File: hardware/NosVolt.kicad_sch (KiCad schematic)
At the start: 10 parts, among them J101 INPUTS, J102 OUTPUTS, SW101 SW_Reset, SW102 SSSS811101, U101 ESP32-S3-WROOM-1

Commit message: Fixes
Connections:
- no-connect marks 0 -> 6
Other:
- sheet USB_LDO ports: added 5V; removed none
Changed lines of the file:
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@@
 		(color 0 0 0 0)
 	)
+	(no_connect
+		(at 137.16 147.32)
+	)
+	(no_connect
+		(at 62.23 74.93)
+	)
+	(no_connect
+		(at 68.58 118.11)
+	)
+	(no_connect
+		(at 68.58 143.51)
+	)
+	(no_connect
+		(at 137.16 173.99)
+	)
+	(no_connect
+		(at 137.16 121.92)
+	)
 	(wire
 		(pts
@@
 	(wire
 		(pts
+			(xy 130.81 173.99) (xy 137.16 173.99)
+		)
+		(stroke
+			(width 0)
+			(type default)
+		)
+	)
+	(wire
+		(pts
 			(xy 67.31 147.32) (xy 82.55 147.32)
 		)
@@
 	(wire
 		(pts
+			(xy 130.81 147.32) (xy 137.16 147.32)
+		)
+		(stroke
+			(width 0)
+			(type default)
+		)
+	)
+	(wire
+		(pts
 			(xy 69.85 163.83) (xy 69.85 149.86)
 		)
@@
 	(wire
 		(pts
+			(xy 62.23 118.11) (xy 68.58 118.11)
+		)
+		(stroke
+			(width 0)
+			(type default)
+		)
+	)
+	(wire
+		(pts
 			(xy 77.47 85.09) (xy 82.55 85.09)
 		)
@@
 	(wire
 		(pts
+			(xy 62.23 143.51) (xy 68.58 143.51)
+		)
+		(stroke
+			(width 0)
+			(type default)
+		)
+	)
+	(wire
+		(pts
 			(xy 260.35 52.07) (xy 270.51 52.07)
 		)
@@
 	(wire
 		(pts
+			(xy 55.88 74.93) (xy 62.23 74.93)
+		)
+		(stroke
+			(width 0)
+			(type default)
+		)
+	)
+	(wire
+		(pts
 			(xy 88.9 121.92) (xy 88.9 147.32)
 		)
@@
 	(wire
 		(pts
+			(xy 130.81 121.92) (xy 137.16 121.92)
+		)
+		(stroke
+			(width 0)
+			(type default)
+		)
+	)
+	(wire
+		(pts
 			(xy 57.15 36.83) (xy 57.15 35.56)
 		)
@@
 	)
 	(sheet
-		(at 43.18 74.93)
-		(size 12.7 10.16)
+		(at 43.18 72.39)
+		(size 12.7 12.7)
 		(exclude_from_sim no)
 		(in_bom yes)
@@
 		)
 		(property "Sheetname" "USB_LDO"
-			(at 43.18 70.866 0)
+			(at 43.18 68.326 0)
 			(effects
 				(font
@@
 		)
 		(property "Sheetfile" "USB_LDO.kicad_sch"
-			(at 42.672 72.39 0)
+			(at 42.672 69.85 0)
 			(effects
 				(font
@@
 			(effects
 				(font
+					(size 1.27 1.27)
+				)
+				(justify right)
+			)
+		)
+		(pin "5V" output
+			(at 55.88 74.93 0)
+			(effects
+				(font

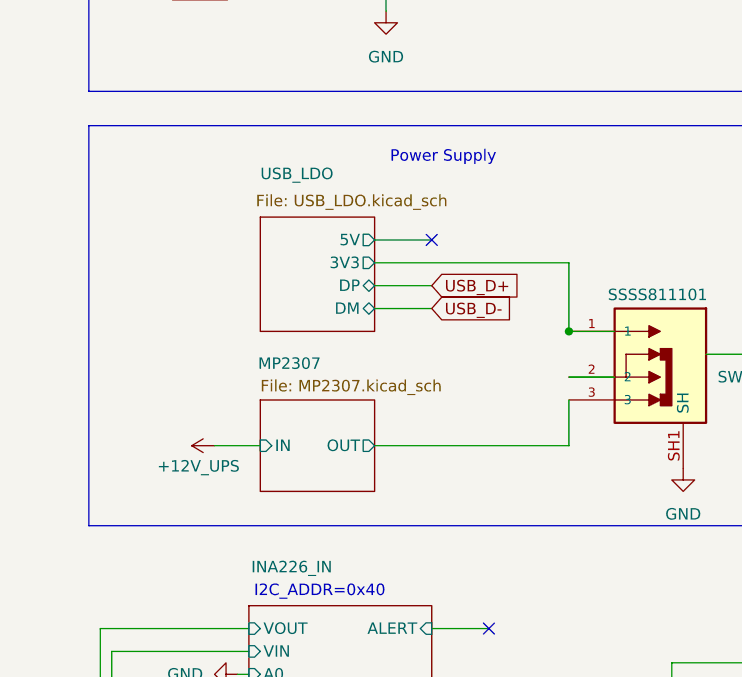
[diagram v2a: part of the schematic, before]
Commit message: ldo optimization
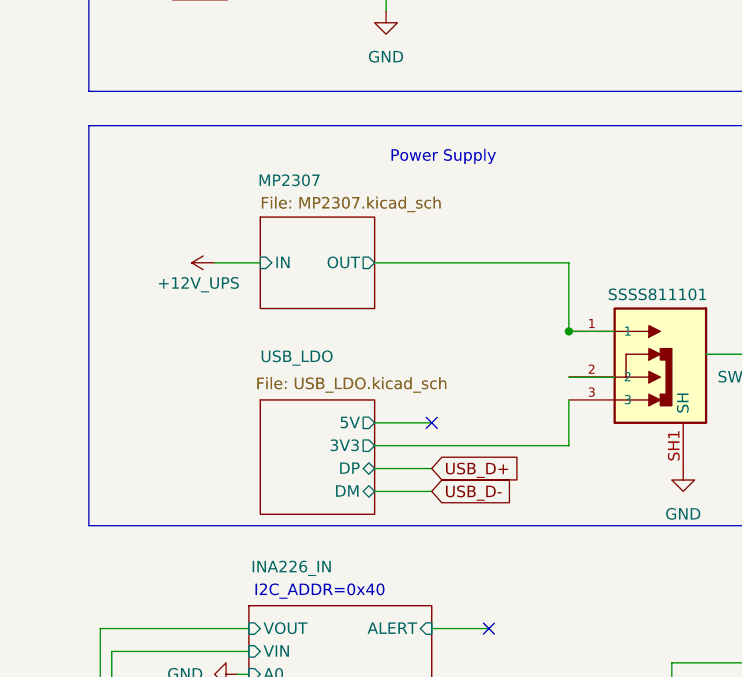
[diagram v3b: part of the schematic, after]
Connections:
- net MP2307/OUT: now also SW102.1; no longer SW102.3
- net USB_LDO/3V3: now also SW102.3; no longer SW102.1
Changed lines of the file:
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@@
 	)
 	(no_connect
-		(at 62.23 74.93)
+		(at 62.23 95.25)
 	)
 	(no_connect
@@
 	(wire
 		(pts
-			(xy 38.1 97.79) (xy 43.18 97.79)
-		)
-		(stroke
-			(width 0)
-			(type default)
-		)
-	)
-	(wire
-		(pts
-			(xy 55.88 77.47) (xy 77.47 77.47)
-		)
-		(stroke
-			(width 0)
-			(type default)
-		)
-	)
-	(wire
-		(pts
 			(xy 140.97 71.12) (xy 137.16 71.12)
 		)
@@
 	(wire
 		(pts
-			(xy 55.88 82.55) (xy 62.23 82.55)
+			(xy 55.88 102.87) (xy 62.23 102.87)
 		)
 		(stroke
@@
 	(wire
 		(pts
+			(xy 38.1 77.47) (xy 43.18 77.47)
+		)
+		(stroke
+			(width 0)
+			(type default)
+		)
+	)
+	(wire
+		(pts
 			(xy 77.47 90.17) (xy 82.55 90.17)
 		)
@@
 	(wire
 		(pts
-			(xy 55.88 74.93) (xy 62.23 74.93)
+			(xy 55.88 95.25) (xy 62.23 95.25)
 		)
 		(stroke
@@
 	(wire
 		(pts
-			(xy 55.88 80.01) (xy 62.23 80.01)
+			(xy 55.88 100.33) (xy 62.23 100.33)
 		)
 		(stroke
@@
 	(wire
 		(pts
+			(xy 55.88 77.47) (xy 77.47 77.47)
+		)
+		(stroke
+			(width 0)
+			(type default)
+		)
+	)
+	(wire
+		(pts
 			(xy 57.15 36.83) (xy 57.15 35.56)
 		)
@@
 	(global_label "USB_D+"
 		(shape input)
-		(at 62.23 80.01 0)
+		(at 62.23 100.33 0)
 		(fields_autoplaced yes)
 		(effects
@@
 		)
 		(property "Intersheetrefs" "${INTERSHEET_REFS}"
-			(at 72.8352 80.01 0)
+			(at 72.8352 100.33 0)
 			(effects
 				(font
@@
 	(global_label "USB_D-"
 		(shape input)
-		(at 62.23 82.55 0)
+		(at 62.23 102.87 0)
 		(fields_autoplaced yes)
 		(effects
@@
 		)
 		(property "Intersheetrefs" "${INTERSHEET_REFS}"
-			(at 72.8352 82.55 0)
+			(at 72.8352 102.87 0)
 			(effects
 				(font
@@
 	(symbol
 		(lib_id "power:+12V")
-		(at 38.1 97.79 90)
+		(at 38.1 77.47 90)
 		(unit 1)
 		(exclude_from_sim no)
@@
 		(dnp no)
 		(property "Reference" "#PWR0101"
-			(at 41.91 97.79 0)
+			(at 41.91 77.47 0)
 			(effects
 				(font
@@
 		)
 		(property "Value" "+12V_UPS"
-			(at 40.894 100.076 90)
+			(at 40.894 79.756 90)
 			(effects
 				(font
@@
 		)
 		(property "Footprint" ""
-			(at 38.1 97.79 0)
+			(at 38.1 77.47 0)
 			(effects
 				(font
@@
 		)
 		(property "Datasheet" ""
-			(at 38.1 97.79 0)
+			(at 38.1 77.47 0)
 			(effects
 				(font
@@
 		)
 		(property "Description" "Power symbol creates a global label with name \"+12V\""
-			(at 38.1 97.79 0)
+			(at 38.1 77.47 0)
 			(effects
 				(font
@@
 	)
 	(sheet
-		(at 43.18 92.71)
+		(at 43.18 72.39)
 		(size 12.7 10.16)
 		(exclude_from_sim no)
@@
 		)
 		(property "Sheetname" "MP2307"
-			(at 42.926 89.408 0)
+			(at 42.926 69.088 0)
 			(effects
 				(font
@@
 		)
 		(property "Sheetfile" "MP2307.kicad_sch"
-			(at 43.18 90.424 0)
+			(at 43.18 70.104 0)
 			(effects
 				(font
@@
 		)
 		(pin "IN" input
-			(at 43.18 97.79 180)
+			(at 43.18 77.47 180)
 			(effects
 				(font
@@
 		)
 		(pin "OUT" output
-			(at 55.88 97.79 0)
+			(at 55.88 77.47 0)
 			(effects
 				(font
@@
 	)
 	(sheet
-		(at 43.18 72.39)
+		(at 43.18 92.71)
 		(size 12.7 12.7)
 		(exclude_from_sim no)
@@
 		)
 		(property "Sheetname" "USB_LDO"
-			(at 43.18 68.326 0)
+			(at 43.18 88.646 0)
 			(effects
 				(font
@@
 		)
 		(property "Sheetfile" "USB_LDO.kicad_sch"
-			(at 42.672 69.85 0)
+			(at 42.672 90.17 0)
 			(effects
 				(font
@@
 		)
 		(pin "DP" bidirectional
-			(at 55.88 80.01 0)
+			(at 55.88 100.33 0)
 			(effects
 				(font
@@
 		)
 		(pin "DM" bidirectional
-			(at 55.88 82.55 0)
+			(at 55.88 102.87 0)
 			(effects
 				(font
@@
 		)
 		(pin "3V3" output
-			(at 55.88 77.47 0)
+			(at 55.88 97.79 0)
 			(effects
 				(font
@@
 		)
 		(pin "5V" output
-			(at 55.88 74.93 0)
+			(at 55.88 95.25 0)
 			(effects
 				(font

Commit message: Add screen
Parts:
- added U102: GMT028-05, NosLib:GMT028-05, symbol NosLib:GMT028-05
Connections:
- net USB_LDO/3V3 is gone; now on net MP2307/OUT: SW102.3
- net +12V_UPS: now also J101.1 (Pin_1); no longer J101.5 (Pin_5)
- net +3.3V: now also SW102.2, U102.2 (VCC)
- net GND: now also J101.2 (Pin_2), U102.1 (GND); no longer J101.6 (Pin_6)
- net INA226_IN/VIN: now also J101.6 (Pin_6); no longer J101.2 (Pin_2)
- net INA226_IN/VOUT: now also J101.5 (Pin_5); no longer J101.1 (Pin_1)
- net MP2307/OUT: no longer SW102.1
- net SPI_CS_TFT: now reaches U101.18 (GPIO10/TOUCH10/ADC1_CH9/FSPICS0/FSPIIO4/SUBSPICS0)
- net SPI_CS_TFT: now also U102.7 (CS)
- net SPI_MOSI: now reaches U101.19 (GPIO11/TOUCH11/ADC2_CH0/FSPID/FSPIIO5/SUBSPID)
- net SPI_MOSI: now also U102.4 (SDA)
- net SPI_SCLK: now reaches U101.20 (GPIO12/TOUCH12/ADC2_CH1/FSPICLK/FSPIIO6/SUBSPICLK)
- net SPI_SCLK: now also U102.3 (SCK)
- net TFT_DC: now reaches U101.21 (GPIO13/TOUCH13/ADC2_CH2/FSPIQ/FSPIIO7/SUBSPIQ)
- net TFT_DC: now also U102.6 (DC)
- net TFT_RST: now reaches U101.22 (GPIO14/TOUCH14/ADC2_CH3/FSPIWP/FSPIDQS/SUBSPIWP)
- net TFT_RST: now also U102.5 (RST)
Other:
- sheet USB_LDO ports: added USB_3V3, USB_5V; removed 3V3, 5V

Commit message: rc
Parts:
- added H101, H102, H103, H104: MountingHole, MountingHole_3.2mm_M3_Pad_Via, symbol Mechanical:MountingHole_Pad
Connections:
- net EN_OUT1: now also U101.28 (SPIIO6/GPIO35/FSPID/SUBSPID); no longer U101.4 (GPIO4/TOUCH4/ADC1_CH3)
- net EN_OUT2: now also U101.29 (SPIIO7/GPIO36/FSPICLK/SUBSPICLK); no longer U101.5 (GPIO5/TOUCH5/ADC1_CH4)
- net EN_OUT3: now also U101.30 (SPIDQS/GPIO37/FSPIQ/SUBSPIQ); no longer U101.6 (GPIO6/TOUCH6/ADC1_CH5)
- net GND: now also H101.1, H102.1, H103.1, H104.1
- net USB_LDO/USB_3V3: now also SW102.1

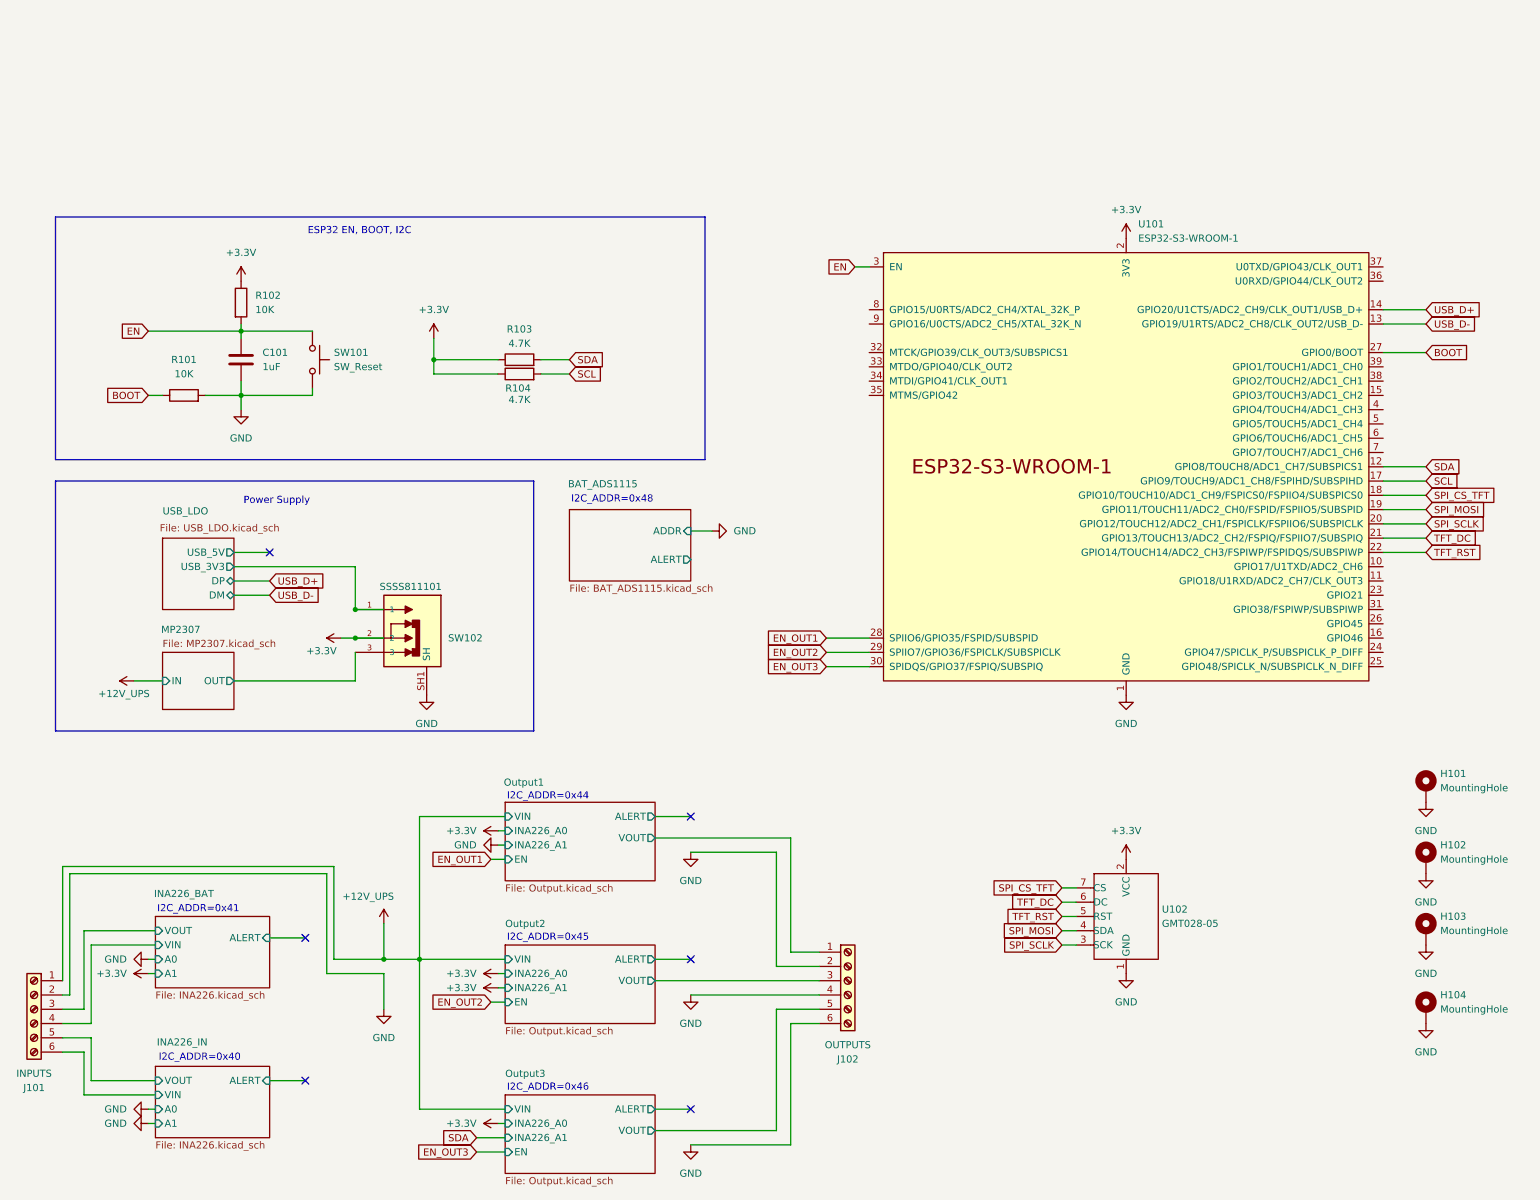
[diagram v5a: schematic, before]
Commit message: esp32 c3 mini
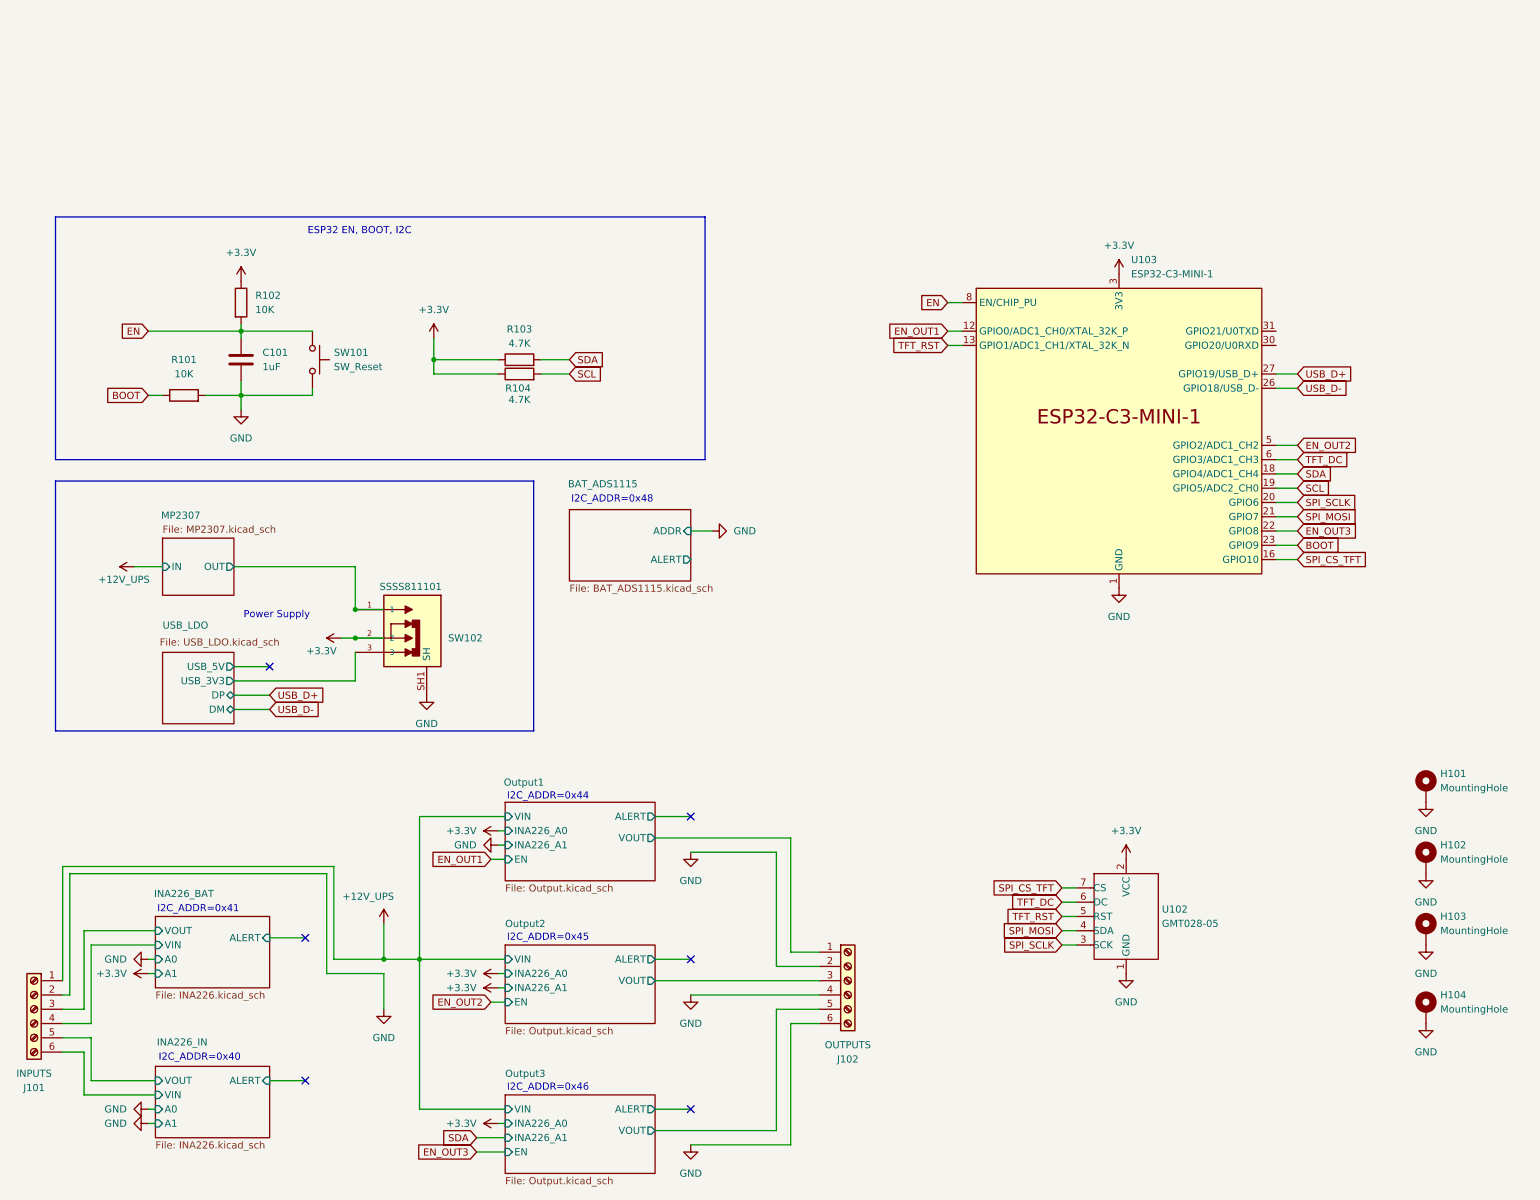
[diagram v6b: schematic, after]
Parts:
- removed U101: ESP32-S3-WROOM-1, PCM_Espressif:ESP32-S3-WROOM-1, symbol PCM_Espressif:ESP32-S3-WROOM-1
- added U103: ESP32-C3-MINI-1, PCM_Espressif:ESP32-C3-MINI-1, symbol PCM_Espressif:ESP32-C3-MINI-1
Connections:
- net +3.3V: now also U103.3 (3V3)
- net BOOT: now also U103.23 (GPIO9)
- net EN: now also U103.8 (EN/CHIP_PU)
- net EN_OUT1: now also U103.12 (GPIO0/ADC1_CH0/XTAL_32K_P)
- net EN_OUT2: now also U103.5 (GPIO2/ADC1_CH2)
- net EN_OUT3: now also U103.22 (GPIO8)
- net GND: now also U103.1 (GND), U103.11 (GND), U103.14 (GND), U103.2 (GND), U103.36 (GND), U103.37 (GND), U103.38 (GND), U103.39 (GND), U103.40 (GND), U103.41 (GND), U103.42 (GND), U103.43 (GND), U103.44 (GND), U103.45 (GND), U103.46 (GND), U103.47 (GND), U103.48 (GND), U103.49 (GND), U103.50 (GND), U103.51 (GND), U103.52 (GND), U103.53 (GND)
- net MP2307/OUT: now also SW102.1; no longer SW102.3
- net SCL: now also U103.19 (GPIO5/ADC2_CH0)
- net SDA: now also U103.18 (GPIO4/ADC1_CH4)
- net SPI_CS_TFT: now also U103.16 (GPIO10)
- net SPI_MOSI: now also U103.21 (GPIO7)
- net SPI_SCLK: now also U103.20 (GPIO6)
- net TFT_DC: now also U103.6 (GPIO3/ADC1_CH3)
- net TFT_RST: now also U103.13 (GPIO1/ADC1_CH1/XTAL_32K_N)
- net USB_D+: now also U103.27 (GPIO19/USB_D+)
- net USB_D-: now also U103.26 (GPIO18/USB_D-)
- net USB_LDO/USB_3V3: now also SW102.3; no longer SW102.1
